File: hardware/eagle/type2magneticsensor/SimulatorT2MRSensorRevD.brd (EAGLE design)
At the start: 48.3 x 30.5 mm, 12 parts, among them U1A 2SS52MOFFSET, U1B 2SS52MOFFSET

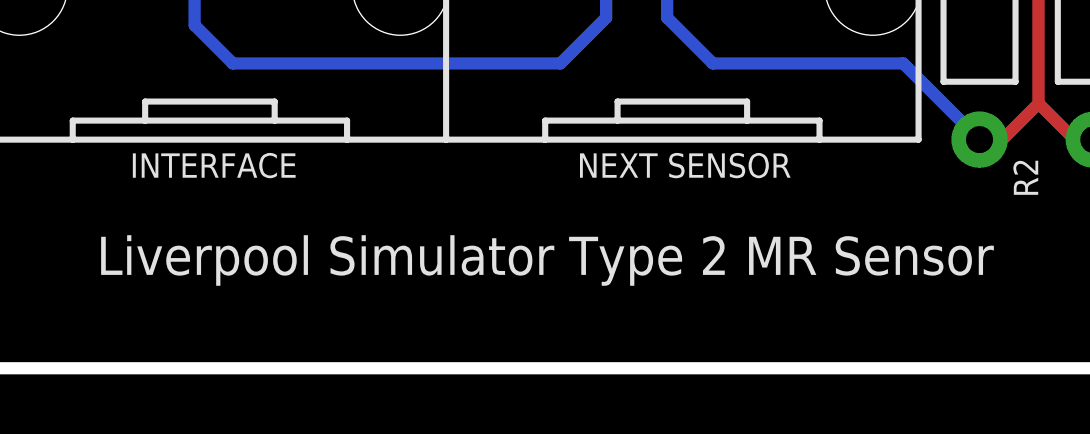
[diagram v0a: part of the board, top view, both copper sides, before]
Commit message: Board Housekeeping
URL on silkscreens, caution messages, tidy up naming conventions.
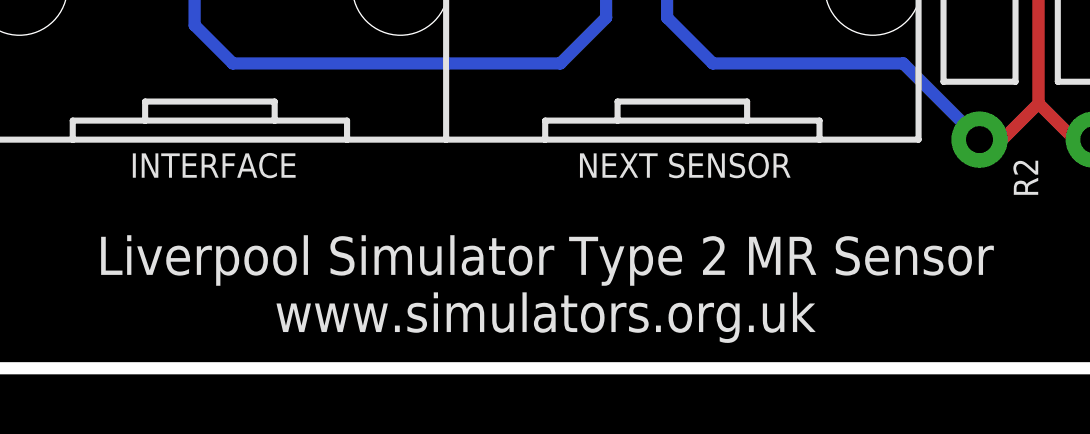
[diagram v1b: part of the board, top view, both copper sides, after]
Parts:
- added U$1: (no value), AIC_Custom:WARNING_TRIANGLE_TPLACE
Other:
- board text added: "Connect this board to Liverpool Simulator Type 2 or compatible equipment ONLY. Refer to documentation for details."
- board text added: "Liverpool Simulator Type 2 MR Sensor www.simulators.org.uk"
- board text removed: "Liverpool Simulator Type 2 MR Sensor"
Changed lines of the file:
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@@
 <board>
 <plain>
-<text x="27.432" y="4.3815" size="1.27" layer="21" font="vector" rot="R180" align="bottom-center">Liverpool Simulator Type 2 MR Sensor</text>
+<text x="27.432" y="4.3815" size="1.27" layer="21" font="vector" rot="R180" align="bottom-center">Liverpool Simulator Type 2 MR Sensor
+www.simulators.org.uk</text>
 <text x="4.699" y="2.54" size="0.762" layer="21" font="vector" rot="R180" align="center">Rev D
 09/2018</text>
@@
 <wire x1="0" y1="2.54" x2="0" y2="27.94" width="0.4064" layer="20"/>
 <wire x1="0" y1="27.94" x2="2.54" y2="30.48" width="0.4064" layer="20" curve="-90"/>
-<wire x1="21.59" y1="0" x2="21.59" y2="7.3152" width="0.254" layer="22" style="shortdash"/>
-<wire x1="21.59" y1="7.3152" x2="26.67" y2="7.3152" width="0.254" layer="22" style="shortdash"/>
-<wire x1="26.67" y1="7.3152" x2="26.67" y2="0" width="0.254" layer="22" style="shortdash"/>
-<wire x1="21.59" y1="7.3152" x2="21.59" y2="9.8552" width="0.254" layer="22" style="shortdash"/>
-<wire x1="21.59" y1="9.8552" x2="26.67" y2="9.8552" width="0.254" layer="22" style="shortdash"/>
-<wire x1="26.67" y1="9.8552" x2="26.67" y2="7.3152" width="0.254" layer="22" style="shortdash"/>
-<text x="24.13" y="3.81" size="0.762" layer="22" font="vector" rot="MR180" align="center">2SS52M
+<wire x1="24.13" y1="30.48" x2="24.13" y2="23.1648" width="0.254" layer="22" style="shortdash"/>
+<wire x1="24.13" y1="23.1648" x2="19.05" y2="23.1648" width="0.254" layer="22" style="shortdash"/>
+<wire x1="19.05" y1="23.1648" x2="19.05" y2="30.48" width="0.254" layer="22" style="shortdash"/>
+<wire x1="24.13" y1="23.1648" x2="24.13" y2="20.6248" width="0.254" layer="22" style="shortdash"/>
+<wire x1="24.13" y1="20.6248" x2="19.05" y2="20.6248" width="0.254" layer="22" style="shortdash"/>
+<wire x1="19.05" y1="20.6248" x2="19.05" y2="23.1648" width="0.254" layer="22" style="shortdash"/>
+<text x="21.59" y="26.67" size="0.762" layer="22" font="vector" rot="MR0" align="center">2SS52M
 Lead
 Forming
 Guide</text>
+<text x="20.32" y="6.35" size="1.016" layer="22" font="vector" rot="MR0" align="center">Connect this board to
+Liverpool Simulator Type 2
+or compatible equipment ONLY.
+Refer to documentation for details.</text>
 </plain>
 <attributes>
@@
 <attribute name="VALUE" x="4.445" y="21.59" size="0.6096" layer="27" font="vector" align="bottom-center"/>
 </element>
+<element name="U$1" library="AIC_Custom" package="WARNING_TRIANGLE_TPLACE" value="" x="38.1" y="3.81" rot="MR0"/>
 </elements>
 <signals>
